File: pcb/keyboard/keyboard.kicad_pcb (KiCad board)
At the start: 2 copper layers, 134.6 x 109.2 mm, 69 parts, among them J1 Audio-Jack-4, J2 sidebutton, SW1 RESET_SW, U1 Arduino_Pro_Micro

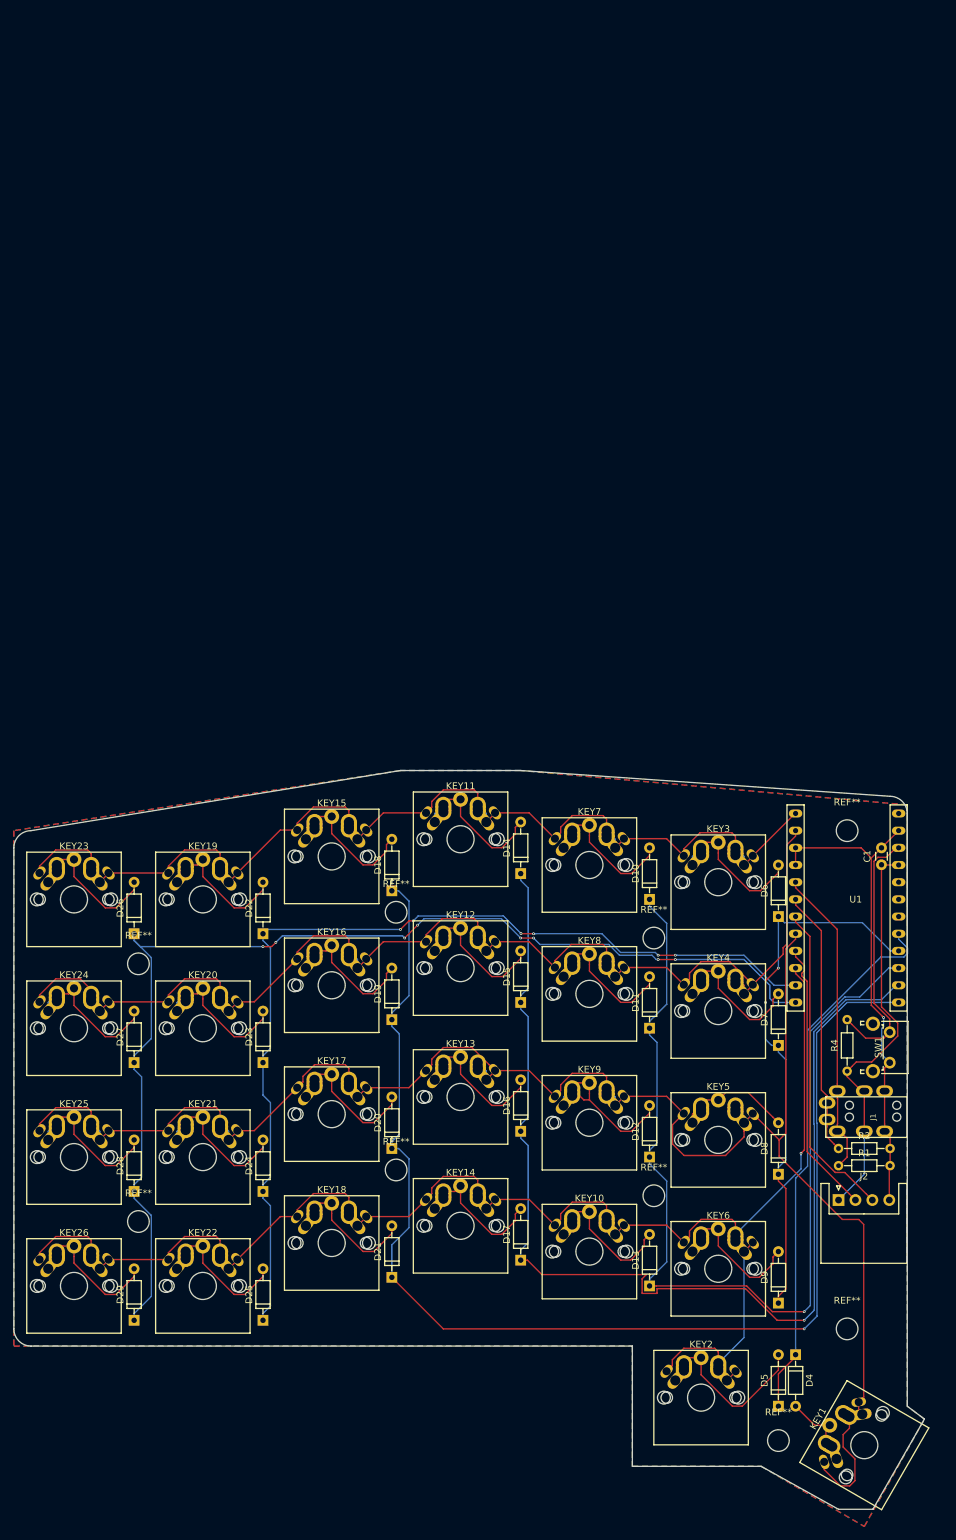
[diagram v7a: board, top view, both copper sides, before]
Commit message: fix pro micro upside donw
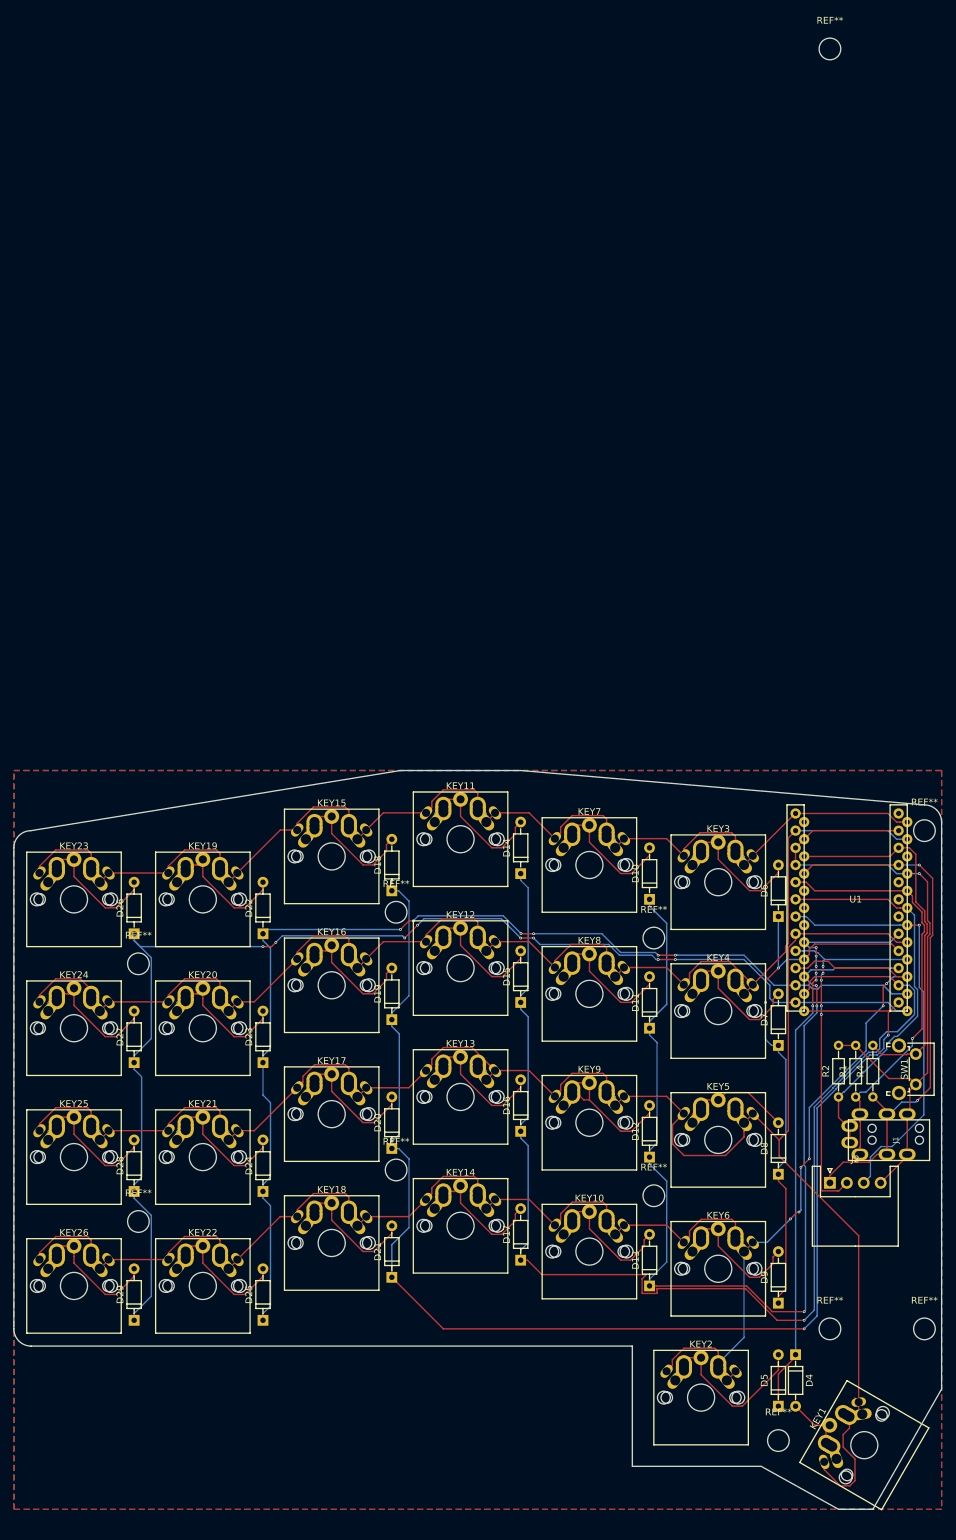
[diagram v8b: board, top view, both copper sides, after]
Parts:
- removed C1: C, Capacitors_THT:C_Disc_D3.0mm_W1.6mm_P2.50mm
- removed the REF** at (123.2, 0.00)
- added REF**: MountingHole_3.2mm_M3, Mounting_Holes:MountingHole_3.2mm_M3, F.Cu at (134.6, 73.7)
- added REF**: MountingHole_3.2mm_M3, Mounting_Holes:MountingHole_3.2mm_M3, F.Cu at (120.7, 73.7)
- added REF**: MountingHole_3.2mm_M3, Mounting_Holes:MountingHole_3.2mm_M3, F.Cu at (134.6, 0.00)
- added U2: Arduino_Pro_Micro, 4x6t2:Arduino_Pro_Micro, B.Cu at (123.2, 12.7)
- moved REF** 189.2 mm to (120.7, -115.6)
- moved R1 10.5 mm to (124.5, 39.4), turned to 90 degrees
- moved R2 7.62 mm to (121.9, 39.4), turned to 90 degrees
- moved R4 5.39 mm to (127.0, 39.4)
- moved SW1 5.03 mm to (133.3, 33.0)
- moved J1 4.78 mm to (135.4, 45.8)
- moved J2 2.84 mm to (120.7, 52.1)
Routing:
- net GND: track 73.1 -> 103.4 mm
- net /ROW4: track 221.5 -> 246.6 mm, vias 1 -> 6
- net +5V: track 60.4 -> 79.6 mm, vias 0 -> 2
- net /SCL: track 39.9 -> 58.4 mm
- net /COL5: track 144.0 -> 161.5 mm
- net /COL3: track 167.6 -> 184.8 mm
- net /ROW1: track 175.6 -> 192.7 mm
- net /COL6: track 168.7 -> 185.7 mm
- net /ROW0: track 155.2 -> 172.1 mm
- net /RST: track 38.5 -> 55.3 mm
- net /ROW2: track 264.6 -> 280.4 mm
- net /SDA: track 46.3 -> 62.0 mm, vias 0 -> 1
- net /X: track 40.8 -> 55.6 mm, vias 0 -> 5
- net /Y: track 47.4 -> 61.8 mm, vias 0 -> 1
- net /COL4: track 186.1 -> 195.0 mm, vias 1 -> 2
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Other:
- board size 134.6 x 109.2 mm -> 137.2 x 109.2 mm
